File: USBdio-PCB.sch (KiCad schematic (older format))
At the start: 1 part

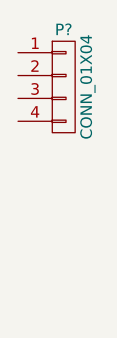
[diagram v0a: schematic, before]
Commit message: added second connector
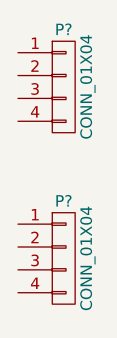
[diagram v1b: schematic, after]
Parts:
- added P?: CONN_01X04, symbol CONN_01X04
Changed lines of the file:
@@
 LIBS:contrib
 LIBS:valves
+LIBS:USBdio-PCB-cache
 EELAYER 25 0
 EELAYER END
@@
 	1    0    0    -1
 $EndComp
+$Comp
+L CONN_01X04 P?
+U 1 1 57ABB785
+P 2750 3800
+F 0 "P?" H 2750 4050 50  0000 C CNN
+F 1 "CONN_01X04" V 2850 3800 50  0000 C CNN
+F 2 "" H 2750 3800 50  0000 C CNN
+F 3 "" H 2750 3800 50  0000 C CNN
+	1    2750 3800
+	1    0    0    -1
+$EndComp

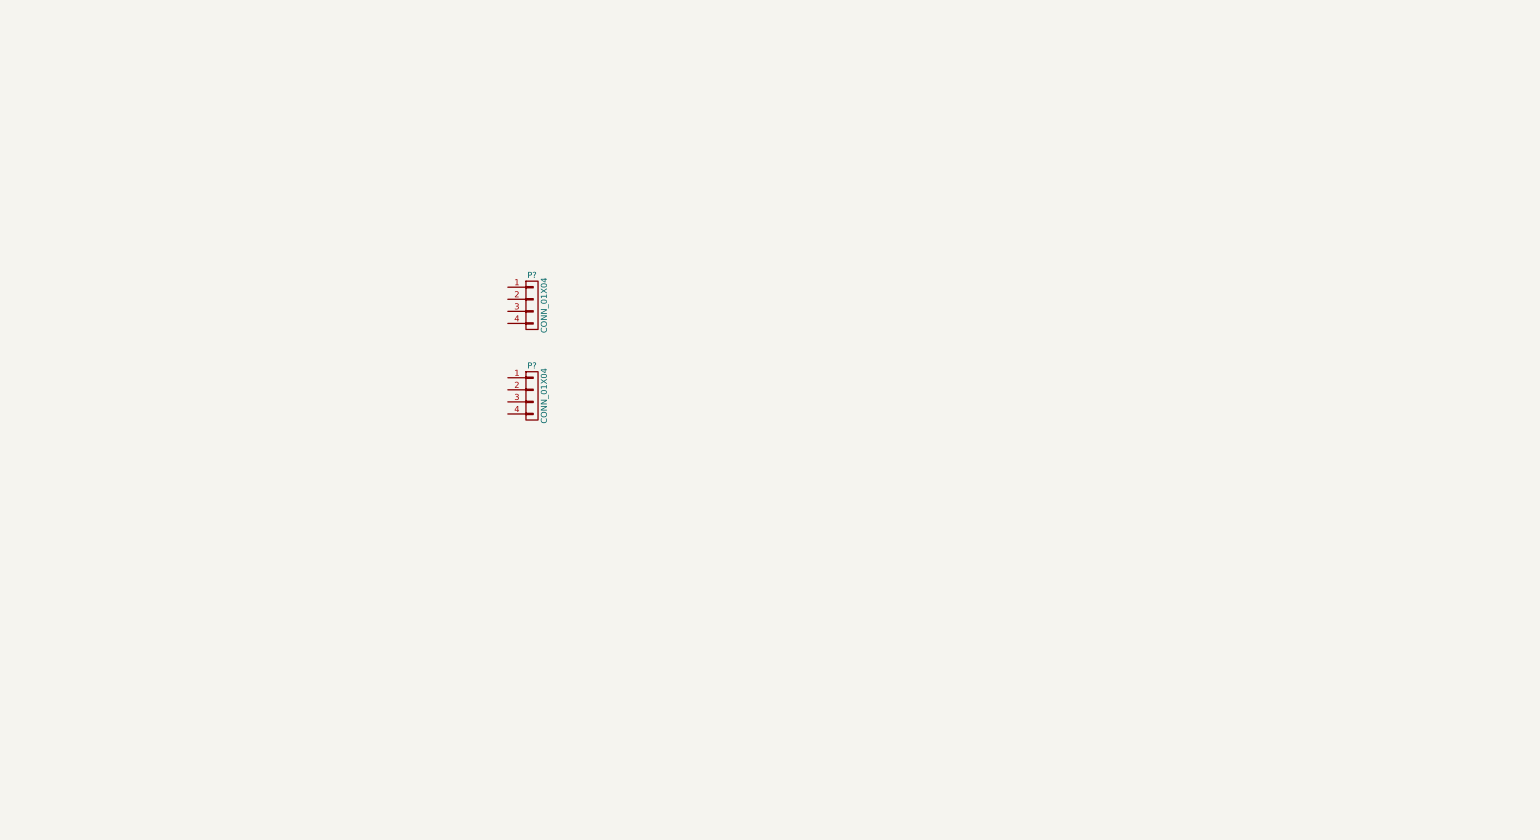
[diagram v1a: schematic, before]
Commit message: finished schematic and created footprint for relay
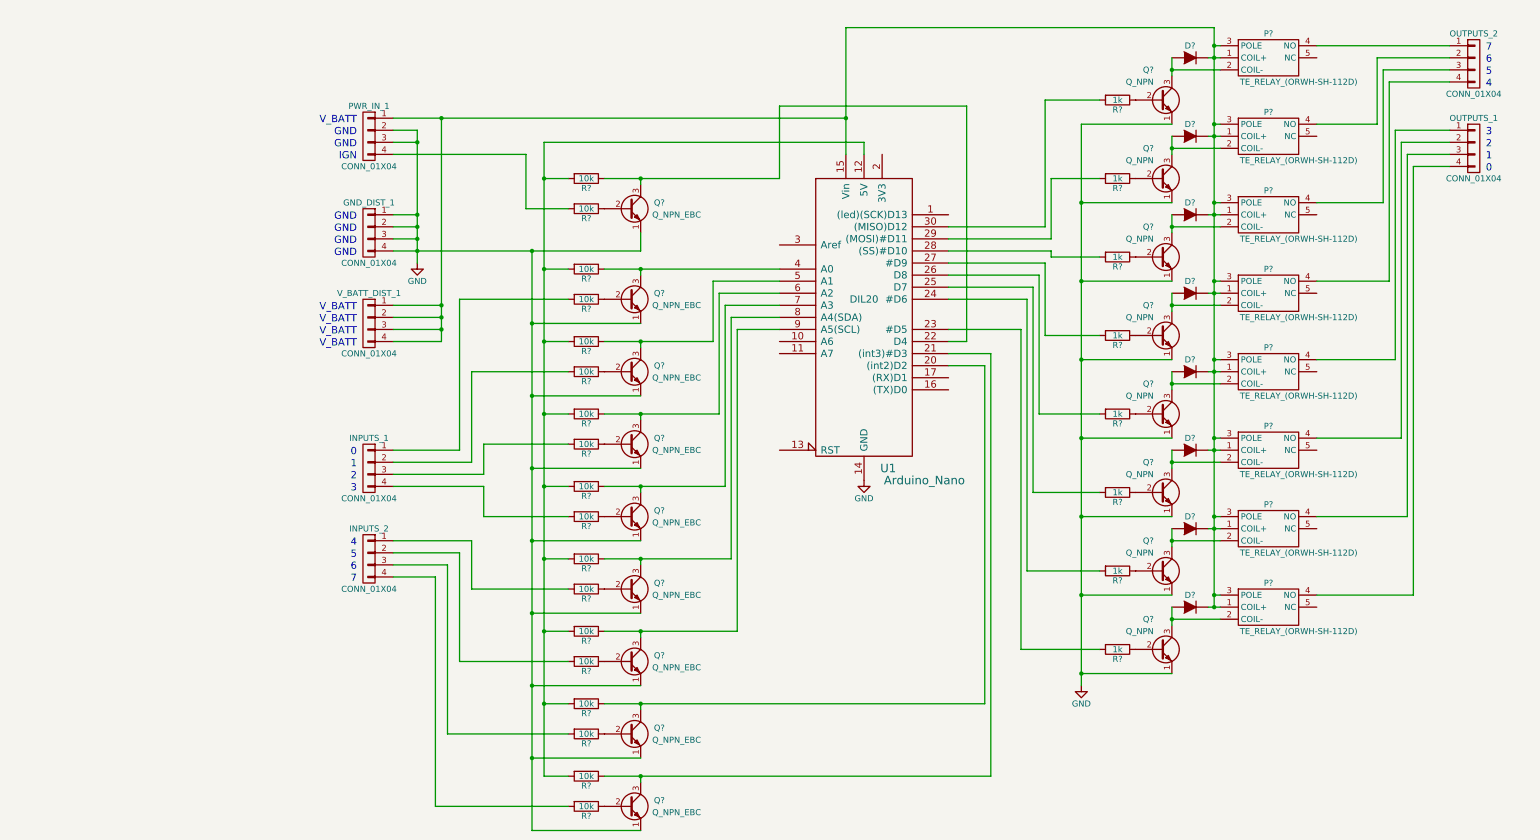
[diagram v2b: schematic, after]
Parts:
- removed P?: CONN_01X04, symbol CONN_01X04
- added D? (x8): D, symbol D
- added GND_DIST_1, INPUTS_1, INPUTS_2, OUTPUTS_1, OUTPUTS_2, V_BATT_DIST_1: CONN_01X04, symbol CONN_01X04
- added P? (x8): TE_RELAY_(ORWH-SH-112D), USBdio-PCB:TE_RELAY_(ORWH-SH-112D), symbol TE_RELAY_(ORWH-SH-112D)
- added Q? (x9): Q_NPN_EBC, symbol Q_NPN_EBC
- added Q? (x8): Q_NPN, symbol Q_NPN_EBC
- added R? (x18): 10k, symbol R
- added R? (x8): 1k, symbol R
- added U1: Arduino_Nano, DIL20, symbol arduino_mini
- gave numbers to parts that had none: 1
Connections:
- net at PWR_IN_1.1 (P1): now also D?.1 (K), D?.1 (K), D?.1 (K), D?.1 (K), D?.1 (K), D?.1 (K), D?.1 (K), D?.1 (K), P?.1 (COIL+), P?.1 (COIL+), P?.1 (COIL+), P?.1 (COIL+), P?.1 (COIL+), P?.1 (COIL+), P?.1 (COIL+), P?.1 (COIL+), P?.3 (POLE), P?.3 (POLE), P?.3 (POLE), P?.3 (POLE), P?.3 (POLE), P?.3 (POLE), P?.3 (POLE), P?.3 (POLE), U1.15 (Vin), V_BATT_DIST_1.1 (P1), V_BATT_DIST_1.2 (P2), V_BATT_DIST_1.3 (P3), V_BATT_DIST_1.4 (P4)
- net GND: now reaches PWR_IN_1.2 (P2)
- net GND: now also PWR_IN_1.3 (P3), GND_DIST_1.1 (P1), GND_DIST_1.2 (P2), GND_DIST_1.3 (P3), GND_DIST_1.4 (P4), Q?.1 (E), Q?.1 (E), Q?.1 (E), Q?.1 (E), Q?.1 (E), Q?.1 (E), Q?.1 (E), Q?.1 (E), Q?.1 (E), Q?.1 (E), Q?.1 (E), Q?.1 (E), Q?.1 (E), Q?.1 (E), Q?.1 (E), Q?.1 (E), Q?.1 (E), U1.14 (GND), U1.19 (GND)
- net at PWR_IN_1.4 (P4): now also R?.2
- new net: R?.2, R?.2, R?.2, R?.2, R?.2, R?.2, R?.2, R?.2, R?.2, U1.12 (5V)
- new net: Q?.3 (C), R?.1, U1.20 ((int2)D2)
- new net: Q?.3 (C), R?.1, U1.21 ((int3)#D3)
- new net: Q?.3 (C), R?.1, U1.22 (D4)
- new net: R?.2, U1.23 (#D5)
- new net: R?.2, U1.24 (#D6)
- new net: R?.2, U1.25 (D7)
- new net: R?.2, U1.26 (D8)
- new net: R?.2, U1.27 (#D9)
- new net: R?.2, U1.28 ((SS)#D10)
- new net: R?.2, U1.29 ((MOSI)#D11)
- new net: R?.2, U1.30 ((MISO)D12)
- new net: Q?.3 (C), R?.1, U1.4 (A0)
- new net: Q?.3 (C), R?.1, U1.5 (A1)
- new net: Q?.3 (C), R?.1, U1.6 (A2)
- new net: Q?.3 (C), R?.1, U1.7 (A3)
- new net: Q?.3 (C), R?.1, U1.8 (A4(SDA))
- new net: Q?.3 (C), R?.1, U1.9 (A5(SCL))
- new net: OUTPUTS_2.1 (P1), P?.4 (NO)
- new net: OUTPUTS_2.2 (P2), P?.4 (NO)
- new net: OUTPUTS_2.3 (P3), P?.4 (NO)
- new net: OUTPUTS_2.4 (P4), P?.4 (NO)
- new net: OUTPUTS_1.1 (P1), P?.4 (NO)
- new net: OUTPUTS_1.2 (P2), P?.4 (NO)
- new net: OUTPUTS_1.3 (P3), P?.4 (NO)
- new net: OUTPUTS_1.4 (P4), P?.4 (NO)
- new net: Q?.2 (B), R?.1 (x17)
- new net: INPUTS_1.1 (P1), R?.2
- new net: INPUTS_1.2 (P2), R?.2
- new net: INPUTS_1.3 (P3), R?.2
- new net: INPUTS_1.4 (P4), R?.2
- new net: INPUTS_2.1 (P1), R?.2
- new net: INPUTS_2.2 (P2), R?.2
- new net: INPUTS_2.3 (P3), R?.2
- new net: INPUTS_2.4 (P4), R?.2
- new net: D?.2 (A), P?.2 (COIL-), Q?.3 (C) (x8)
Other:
- note added: "0"
- note added: "1"
- note added: "2"
- note added: "3"
- note added: "4"
- note added: "5"
- note added: "6"
- note added: "7"
- note added: "GND"
- note added: "IGN"
- note added: "V_BATT"
- moved on the sheet: PWR_IN_1

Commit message: added remainder of footprints and 3D
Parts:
- D1, D2, D3, D4, D5, D6, D7, D8: renamed from D?; footprint (none) -> Diodes_ThroughHole:Diode_DO-41_SOD81_Horizontal_RM10
- GND_DIST_1, INPUTS_1, INPUTS_2, OUTPUTS_1, OUTPUTS_2, PWR_IN_1, V_BATT_DIST_1: footprint (none) -> USBdio-PCB:PHX_HDR_4_POS_(1933202)
- Q1, Q10, Q11, Q12, Q13, Q14, Q15, Q16, Q17, Q2, Q3, Q4, Q5, Q6, Q7, Q8, Q9: renamed from Q?; footprint (none) -> TO_SOT_Packages_THT:TO-92_Molded_Narrow
- R1, R10, R11, R12, R13, R14, R15, R16, R17, R18, R19, R2, R20, R21, R22, R23, R24, R25, R26, R3, R4, R5, R6, R7, R8, R9: renamed from R?; footprint (none) -> Resistors_ThroughHole:Resistor_Horizontal_RM10mm
- U1: footprint DIL20 -> USBdio-PCB:ARDUINO_NANO
- gave numbers to parts that had none: 8

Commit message: started laying out footprints
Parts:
- renumbered P8 to P0, P7 to P1, P6 to P2, P5 to P3, P3 to P5, P2 to P6, P1 to P7
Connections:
- net at OUTPUTS_2.1 (P1): now also P4.4 (NO); no longer P7.4 (NO)
- net at OUTPUTS_2.2 (P2): now also P5.4 (NO); no longer P6.4 (NO)
- net at OUTPUTS_2.3 (P3): now also P6.4 (NO); no longer P5.4 (NO)
- net at OUTPUTS_2.4 (P4): now also P7.4 (NO); no longer P4.4 (NO)
- net at OUTPUTS_1.1 (P1): now also P0.4 (NO); no longer P3.4 (NO)
- net at OUTPUTS_1.2 (P2): now also P1.4 (NO); no longer P2.4 (NO)
- net at OUTPUTS_1.3 (P3): now also P2.4 (NO); no longer P1.4 (NO)
- net at OUTPUTS_1.4 (P4): now also P3.4 (NO); no longer P0.4 (NO)
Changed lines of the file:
@@
 F 3 "" H 10550 1050 50  0000 C CNN
 	1    10550 1050
-	1    0    0    -1
+	1    0    0    1
 $EndComp
 Text Notes 10650 950  0    60   ~ 0
@@
 F 3 "" H 10550 1750 50  0000 C CNN
 	1    10550 1750
-	1    0    0    -1
+	1    0    0    1
 $EndComp
 Text Notes 10650 1650 0    60   ~ 0
@@
 $EndComp
 $Comp
-L TE_RELAY_(ORWH-SH-112D) P1
+L TE_RELAY_(ORWH-SH-112D) P7
 U 1 1 57C43234
 P 8850 1000
-F 0 "P1" H 8850 1200 50  0000 C CNN
+F 0 "P7" H 8850 1200 50  0000 C CNN
 F 1 "TE_RELAY_(ORWH-SH-112D)" H 9100 800 50  0000 C CNN
 F 2 "USBdio-PCB:TE_RELAY_(ORWH-SH-112D)" H 8850 -200 50  0001 C CNN
@@
 $EndComp
 $Comp
-L TE_RELAY_(ORWH-SH-112D) P2
+L TE_RELAY_(ORWH-SH-112D) P6
 U 1 1 57C4ADCB
 P 8850 1650
-F 0 "P2" H 8850 1850 50  0000 C CNN
+F 0 "P6" H 8850 1850 50  0000 C CNN
 F 1 "TE_RELAY_(ORWH-SH-112D)" H 9100 1450 50  0000 C CNN
 F 2 "USBdio-PCB:TE_RELAY_(ORWH-SH-112D)" H 8850 450 50  0001 C CNN
@@
 $EndComp
 $Comp
-L TE_RELAY_(ORWH-SH-112D) P3
+L TE_RELAY_(ORWH-SH-112D) P5
 U 1 1 57C4AFAE
 P 8850 2300
-F 0 "P3" H 8850 2500 50  0000 C CNN
+F 0 "P5" H 8850 2500 50  0000 C CNN
 F 1 "TE_RELAY_(ORWH-SH-112D)" H 9100 2100 50  0000 C CNN
 F 2 "USBdio-PCB:TE_RELAY_(ORWH-SH-112D)" H 8850 1100 50  0001 C CNN
@@
 $EndComp
 $Comp
-L TE_RELAY_(ORWH-SH-112D) P5
+L TE_RELAY_(ORWH-SH-112D) P3
 U 1 1 57C4C762
 P 8850 3600
-F 0 "P5" H 8850 3800 50  0000 C CNN
+F 0 "P3" H 8850 3800 50  0000 C CNN
 F 1 "TE_RELAY_(ORWH-SH-112D)" H 9100 3400 50  0000 C CNN
 F 2 "USBdio-PCB:TE_RELAY_(ORWH-SH-112D)" H 8850 2400 50  0001 C CNN
@@
 $EndComp
 $Comp
-L TE_RELAY_(ORWH-SH-112D) P6
+L TE_RELAY_(ORWH-SH-112D) P2
 U 1 1 57C4C784
 P 8850 4250
-F 0 "P6" H 8850 4450 50  0000 C CNN
+F 0 "P2" H 8850 4450 50  0000 C CNN
 F 1 "TE_RELAY_(ORWH-SH-112D)" H 9100 4050 50  0000 C CNN
 F 2 "USBdio-PCB:TE_RELAY_(ORWH-SH-112D)" H 8850 3050 50  0001 C CNN
@@
 $EndComp
 $Comp
-L TE_RELAY_(ORWH-SH-112D) P7
+L TE_RELAY_(ORWH-SH-112D) P1
 U 1 1 57C4C7A6
 P 8850 4900
-F 0 "P7" H 8850 5100 50  0000 C CNN
+F 0 "P1" H 8850 5100 50  0000 C CNN
 F 1 "TE_RELAY_(ORWH-SH-112D)" H 9100 4700 50  0000 C CNN
 F 2 "USBdio-PCB:TE_RELAY_(ORWH-SH-112D)" H 8850 3700 50  0001 C CNN
@@
 $EndComp
 $Comp
-L TE_RELAY_(ORWH-SH-112D) P8
+L TE_RELAY_(ORWH-SH-112D) P0
 U 1 1 57C4C7C8
 P 8850 5550
-F 0 "P8" H 8850 5750 50  0000 C CNN
+F 0 "P0" H 8850 5750 50  0000 C CNN
 F 1 "TE_RELAY_(ORWH-SH-112D)" H 9100 5350 50  0000 C CNN
 F 2 "USBdio-PCB:TE_RELAY_(ORWH-SH-112D)" H 8850 4350 50  0001 C CNN

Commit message: initial commit of deutsch enclosure layout
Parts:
- removed U1: Arduino_Nano, USBdio-PCB:ARDUINO_NANO, symbol arduino_mini
- added CONN_1: DEUTSCH_CONN_(DTM13-12PA-12PB-R008), USBdio-PCB:DEUTSCH_CONN_(DTM13-12PA-12PB-R008), symbol DEUTSCH_CONN_(DTM13-12PA-12PB-R008)
- added IC1: ATMEGA328-P, Housings_DIP:DIP-28_W7.62mm_LongPads, symbol ATMEGA328-P
- D1, D2, D3, D4, D5, D6, D7, D8: footprint Diodes_ThroughHole:Diode_DO-41_SOD81_Horizontal_RM10 -> Resistors_SMD:R_1206_HandSoldering
- Q1, Q2, Q3, Q4, Q5, Q6, Q7, Q8, Q9: value Q_NPN_EBC -> Q_NPN_BEC; footprint TO_SOT_Packages_THT:TO-92_Molded_Narrow -> TO_SOT_Packages_SMD:SOT-23_Handsoldering; symbol Q_NPN_EBC -> Q_NPN_BEC
- Q10, Q11, Q12, Q13, Q14, Q15, Q16, Q17: footprint TO_SOT_Packages_THT:TO-92_Molded_Narrow -> TO_SOT_Packages_SMD:SOT-23_Handsoldering; symbol Q_NPN_EBC -> Q_NPN_BEC
- R1, R10, R11, R12, R13, R14, R15, R16, R17, R18, R19, R2, R20, R21, R22, R23, R24, R25, R26, R3, R4, R5, R6, R7, R8, R9: footprint Resistors_ThroughHole:Resistor_Horizontal_RM10mm -> Resistors_SMD:R_1206_HandSoldering
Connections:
- net GND: now also Q1.2 (E), Q10.2 (E), Q11.2 (E), Q12.2 (E), Q13.2 (E), Q14.2 (E), Q15.2 (E), Q16.2 (E), Q17.2 (E), Q2.2 (E), Q3.2 (E), Q4.2 (E), Q5.2 (E), Q6.2 (E), Q7.2 (E), Q8.2 (E), Q9.2 (E), IC1.22 (GND), IC1.8 (GND); no longer Q1.1 (E), Q10.1 (E), Q11.1 (E), Q12.1 (E), Q13.1 (E), Q14.1 (E), Q15.1 (E), Q16.1 (E), Q17.1 (E), Q2.1 (E), Q3.1 (E), Q4.1 (E), Q5.1 (E), Q6.1 (E), Q7.1 (E), Q8.1 (E), Q9.1 (E)
- net at Q8.3 (C), R15.1: now also IC1.4 ((PCINT18/INT0)PD2)
- net at Q9.3 (C), R17.1: now also IC1.5 ((PCINT19/OC2B/INT1)PD3)
- net at Q1.3 (C), R1.1: now also IC1.6 ((PCINT20/XCK/T0)PD4)
- net at R26.2: now also IC1.11 ((PCINT21/OC0B/T1)PD5)
- net at R25.2: now also IC1.12 ((PCINT22/OC0A/AIN0)PD6)
- net at R24.2: now also IC1.13 ((PCINT23/AIN1)PD7)
- net at R23.2: now also IC1.14 ((PCINT0/CLKO/ICP1)PB0)
- net at R22.2: now also IC1.15 ((PCINT1/OC1A)PB1)
- net at R21.2: now also IC1.16 ((PCINT2/OC1B/~SS~)PB2)
- net at R20.2: now also IC1.17 ((PCINT3/OC2A/MOSI)PB3)
- net at R19.2: now also IC1.18 ((PCINT4/MISO)PB4)
- net at Q2.3 (C), R3.1: now also IC1.23 ((PCINT8/ADC0)PC0)
- net at Q3.3 (C), R5.1: now also IC1.24 ((PCINT9/ADC1)PC1)
- net at Q4.3 (C), R7.1: now also IC1.25 ((PCINT10/ADC2)PC2)
- net at Q5.3 (C), R9.1: now also IC1.26 ((PCINT11/ADC3)PC3)
- net at Q6.3 (C), R11.1: now also IC1.27 ((PCINT12/SDA/ADC4)PC4)
- net at Q7.3 (C), R13.1: now also IC1.28 ((PCINT13/SCL/ADC5)PC5)
- net at R4.1: now also Q2.1 (B); no longer Q2.2 (B)
- net at R6.1: now also Q3.1 (B); no longer Q3.2 (B)
- net at R8.1: now also Q4.1 (B); no longer Q4.2 (B)
- net at R10.1: now also Q5.1 (B); no longer Q5.2 (B)
- net at R12.1: now also Q6.1 (B); no longer Q6.2 (B)
- net at R14.1: now also Q7.1 (B); no longer Q7.2 (B)
- net at R16.1: now also Q8.1 (B); no longer Q8.2 (B)
- net at R18.1: now also Q9.1 (B); no longer Q9.2 (B)
- net at R2.1: now also Q1.1 (B); no longer Q1.2 (B)
- net at R19.1: now also Q10.1 (B); no longer Q10.2 (B)
- net at R20.1: now also Q11.1 (B); no longer Q11.2 (B)
- net at R21.1: now also Q12.1 (B); no longer Q12.2 (B)
- net at R22.1: now also Q13.1 (B); no longer Q13.2 (B)
- net at R23.1: now also Q14.1 (B); no longer Q14.2 (B)
- net at R24.1: now also Q15.1 (B); no longer Q15.2 (B)
- net at R25.1: now also Q16.1 (B); no longer Q16.2 (B)
- net at R26.1: now also Q17.1 (B); no longer Q17.2 (B)
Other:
- moved on the sheet: D1, D2, D3, D4, D5, D6, D7, D8, GND_DIST_1, INPUTS_1, INPUTS_2, OUTPUTS_1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
